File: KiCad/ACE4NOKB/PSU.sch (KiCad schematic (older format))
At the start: 31 parts, among them IC1 LM7805_TO220

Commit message: Reorder chematics.
Signed-off-by: John Bradley <flypie@rocketmail.com>
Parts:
- removed Z10, Z11, Z9: 74AHCT393, Package_DIP:DIP-14_W7.62mm, symbol 74xx:74LS393
- renumbered IC1 to PR1
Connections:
- wire segments 105 -> 99
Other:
- moved on the sheet: Z101B, Z20E, Z21D, Z22D, Z23E, Z24E, Z25E
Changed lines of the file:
@@
 $Descr A4 11693 8268
 encoding utf-8
-Sheet 6 6
+Sheet 7 8
 Title "ACE4NOKB"
-Date "2019-10-24"
+Date "2020-04-30"
 Rev "Alpha"
 Comp "Ontobus"
@@
 	3150 1825 3275 1825
 Wire Wire Line
-	7850 3025 7525 3025
+	7850 3025 6225 3025
 Wire Wire Line
 	4925 1100 5175 1100
 Wire Wire Line
-	7525 3025 7075 3025
-Connection ~ 7525 3025
-Connection ~ 7075 3025
-Wire Wire Line
-	7075 3025 6625 3025
-Connection ~ 6625 3025
-Wire Wire Line
-	6625 3025 6200 3025
-Connection ~ 6200 3025
-Wire Wire Line
-	6200 3025 5775 3025
+	6225 3025 5775 3025
+Connection ~ 6225 3025
 Connection ~ 5775 3025
+Wire Wire Line
+	5775 3025 5325 3025
 Connection ~ 5325 3025
-Connection ~ 3550 3025
+Wire Wire Line
+	5325 3025 4900 3025
+Connection ~ 4900 3025
+Wire Wire Line
+	4900 3025 4475 3025
+Connection ~ 4475 3025
 Connection ~ 2675 3025
 Wire Wire Line
 	2675 3025 2225 3025
 Wire Wire Line
-	7775 4025 7525 4025
-Connection ~ 7525 4025
-Wire Wire Line
-	7525 4025 7075 4025
-Connection ~ 7075 4025
-Wire Wire Line
-	7075 4025 6625 4025
-Connection ~ 6625 4025
-Wire Wire Line
-	6625 4025 6200 4025
-Connection ~ 6200 4025
-Wire Wire Line
-	6200 4025 5775 4025
+	6475 4025 6225 4025
+Connection ~ 6225 4025
+Wire Wire Line
+	6225 4025 5775 4025
 Connection ~ 5775 4025
+Wire Wire Line
+	5775 4025 5325 4025
 Connection ~ 5325 4025
-Connection ~ 3550 4025
+Wire Wire Line
+	5325 4025 4900 4025
+Connection ~ 4900 4025
+Wire Wire Line
+	4900 4025 4475 4025
+Connection ~ 4475 4025
 Connection ~ 2675 4025
 Wire Wire Line
@@
 	3975 1100 3975 1325
 Wire Wire Line
-	3550 3025 3125 3025
-Wire Wire Line
-	3550 4025 3125 4025
-Wire Wire Line
 	3125 3125 3125 3025
-Connection ~ 3125 3025
 Wire Wire Line
 	3125 3025 2675 3025
 Wire Wire Line
 	3125 3925 3125 4025
-Connection ~ 3125 4025
 Wire Wire Line
 	3125 4025 2675 4025
 Wire Wire Line
-	5775 4025 5325 4025
-Wire Wire Line
-	5775 3025 5325 3025
+	4475 4025 4025 4025
+Wire Wire Line
+	4475 3025 4025 3025
 Wire Wire Line
 	1425 1400 1425 1200
@@
 Connection ~ 1425 1700
 Connection ~ 1425 1825
-Wire Wire Line
-	5325 4025 4900 4025
-Wire Wire Line
-	5325 3025 4900 3025
-Connection ~ 4900 4025
-Wire Wire Line
-	4900 4025 4450 4025
-Connection ~ 4900 3025
-Wire Wire Line
-	4900 3025 4450 3025
-Connection ~ 3975 4025
-Wire Wire Line
-	3975 4025 3550 4025
-Connection ~ 3975 3025
-Wire Wire Line
-	3975 3025 3550 3025
-Connection ~ 4450 4025
-Wire Wire Line
-	4450 4025 3975 4025
-Connection ~ 4450 3025
-Wire Wire Line
-	4450 3025 3975 3025
-$Comp
-L 74xx:74LS393 Z9
-U 3 1 5E382F4F
-P 4900 3525
-F 0 "Z9" H 4975 4125 50  0000 R CNN
-F 1 "74AHCT393" H 5125 4225 50  0000 R CNN
-F 2 "Package_DIP:DIP-14_W7.62mm" H 4900 3525 50  0001 C CNN
-F 3 "74xx\\74LS393.pdf" H 4900 3525 50  0001 C CNN
-	3    4900 3525
-	-1   0    0    1
-$EndComp
 $Comp
 L 74xx:74LS74 Z27
@@
 $EndComp
 $Comp
-L 74xx:74LS393 Z11
-U 3 1 5D2736AB
-P 3550 3525
-F 0 "Z11" H 3650 4125 50  0000 R CNN
-F 1 "74AHCT393" H 3775 4350 50  0000 R CNN
-F 2 "Package_DIP:DIP-14_W7.62mm" H 3550 3525 50  0001 C CNN
-F 3 "74xx\\74LS393.pdf" H 3550 3525 50  0001 C CNN
-	3    3550 3525
-	-1   0    0    1
-$EndComp
-$Comp
-L 74xx:74LS393 Z10
-U 3 1 5D1978A5
-P 3975 3525
-F 0 "Z10" H 3875 4125 50  0000 L CNN
-F 1 "74AHCT393" H 3775 4225 50  0000 L CNN
-F 2 "Package_DIP:DIP-14_W7.62mm" H 3975 3525 50  0001 C CNN
-F 3 "74xx\\74LS393.pdf" H 3975 3525 50  0001 C CNN
-	3    3975 3525
-	-1   0    0    1
-$EndComp
-$Comp
 L 74xx:74LS30 Z101
 U 2 1 6372EB23
-P 4450 3525
-F 0 "Z101" H 4575 4125 50  0000 R CNN
-F 1 "74AHCT30D" H 4650 4350 50  0000 R CNN
-F 2 "Package_SO:SOIC-14_3.9x8.7mm_P1.27mm" H 4450 3525 50  0001 C CNN
-F 3 "http://www.ti.com/lit/gpn/sn74LS21" H 4450 3525 50  0001 C CNN
-F 4 "NEXPERIA" H 4450 3525 50  0001 C CNN "Manufacturer_Name"
-F 5 "74AHCT30D" H 4450 3525 50  0001 C CNN "Manufacturer_Part_Number"
-	2    4450 3525
+P 3575 3525
+F 0 "Z101" H 3700 4125 50  0000 R CNN
+F 1 "74AHCT30D" H 3775 4350 50  0000 R CNN
+F 2 "Package_SO:SOIC-14_3.9x8.7mm_P1.27mm" H 3575 3525 50  0001 C CNN
+F 3 "http://www.ti.com/lit/gpn/sn74LS21" H 3575 3525 50  0001 C CNN
+F 4 "NEXPERIA" H 3575 3525 50  0001 C CNN "Manufacturer_Name"
+F 5 "74AHCT30D" H 3575 3525 50  0001 C CNN "Manufacturer_Part_Number"
+	2    3575 3525
 	-1   0    0    1
 $EndComp
@@
 L 74xx:74LS11 Z22
 U 4 1 6989826C
-P 6625 3525
-F 0 "Z22" H 6700 4125 50  0000 R CNN
-F 1 "74AHCT11" H 6825 4225 50  0000 R CNN
-F 2 "Package_DIP:DIP-14_W7.62mm" H 6625 3525 50  0001 C CNN
-F 3 "http://www.ti.com/lit/gpn/sn74LS11" H 6625 3525 50  0001 C CNN
-	4    6625 3525
+P 5325 3525
+F 0 "Z22" H 5400 4125 50  0000 R CNN
+F 1 "74AHCT11" H 5525 4225 50  0000 R CNN
+F 2 "Package_DIP:DIP-14_W7.62mm" H 5325 3525 50  0001 C CNN
+F 3 "http://www.ti.com/lit/gpn/sn74LS11" H 5325 3525 50  0001 C CNN
+	4    5325 3525
 	-1   0    0    1
 $EndComp
@@
 L 74xx:74LS02 Z24
 U 5 1 629F3A79
-P 5325 3525
-F 0 "Z24" H 5425 4125 50  0000 R CNN
-F 1 "SN74AHCT02N" H 5600 4350 50  0000 R CNN
-F 2 "Package_DIP:DIP-14_W7.62mm" H 5325 3525 50  0001 C CNN
-F 3 "http://www.ti.com/lit/gpn/sn74ls02" H 5325 3525 50  0001 C CNN
-	5    5325 3525
-	-1   0    0    1
-$EndComp
-$Comp
-L Regulator_Linear:LM7805_TO220 IC1
+P 4025 3525
+F 0 "Z24" H 4125 4125 50  0000 R CNN
+F 1 "SN74AHCT02N" H 4300 4350 50  0000 R CNN
+F 2 "Package_DIP:DIP-14_W7.62mm" H 4025 3525 50  0001 C CNN
+F 3 "http://www.ti.com/lit/gpn/sn74ls02" H 4025 3525 50  0001 C CNN
+	5    4025 3525
+	-1   0    0    1
+$EndComp
+$Comp
+L Regulator_Linear:LM7805_TO220 PR1
 U 1 1 735D1281
 P 2650 1100
-F 0 "IC1" H 2675 1375 50  0000 C CNN
+F 0 "PR1" H 2675 1375 50  0000 C CNN
 F 1 "LM7805_TO220" H 2675 1275 50  0000 C CNN
 F 2 "Package_TO_SOT_THT:TO-220-3_Vertical" H 2650 1325 50  0001 C CIN
@@
 L 74xx:74LS86 Z23
 U 5 1 6A760723
-P 7525 3525
-F 0 "Z23" H 7250 3450 50  0000 R CNN
-F 1 "74AHCT86" H 7250 3550 50  0000 R CNN
-F 2 "Package_DIP:DIP-14_W7.62mm" H 7525 3525 50  0001 C CNN
-F 3 "74xx/74ls86.pdf" H 7525 3525 50  0001 C CNN
-	5    7525 3525
+P 6225 3525
+F 0 "Z23" H 5950 3450 50  0000 R CNN
+F 1 "74AHCT86" H 5950 3550 50  0000 R CNN
+F 2 "Package_DIP:DIP-14_W7.62mm" H 6225 3525 50  0001 C CNN
+F 3 "74xx/74ls86.pdf" H 6225 3525 50  0001 C CNN
+	5    6225 3525
 	-1   0    0    1
 $EndComp
@@
 L 74xx:74LS11 Z21
 U 4 1 69DE0CE8
-P 7075 3525
-F 0 "Z21" H 6975 4125 50  0000 L CNN
-F 1 "74AHCT11" H 6875 4350 50  0000 L CNN
-F 2 "Package_DIP:DIP-14_W7.62mm" H 7075 3525 50  0001 C CNN
-F 3 "http://www.ti.com/lit/gpn/sn74LS11" H 7075 3525 50  0001 C CNN
-	4    7075 3525
+P 5775 3525
+F 0 "Z21" H 5675 4125 50  0000 L CNN
+F 1 "74AHCT11" H 5575 4350 50  0000 L CNN
+F 2 "Package_DIP:DIP-14_W7.62mm" H 5775 3525 50  0001 C CNN
+F 3 "http://www.ti.com/lit/gpn/sn74LS11" H 5775 3525 50  0001 C CNN
+	4    5775 3525
 	-1   0    0    1
 $EndComp
@@
 L 74xx:74LS02 Z25
 U 5 1 67CF6A6D
-P 5775 3525
-F 0 "Z25" H 5875 4125 50  0000 R CNN
-F 1 "74AHCT02" H 5975 4225 50  0000 R CNN
-F 2 "Package_DIP:DIP-14_W7.62mm" H 5775 3525 50  0001 C CNN
-F 3 "http://www.ti.com/lit/gpn/sn74ls02" H 5775 3525 50  0001 C CNN
-	5    5775 3525
+P 4475 3525
+F 0 "Z25" H 4575 4125 50  0000 R CNN
+F 1 "74AHCT02" H 4675 4225 50  0000 R CNN
+F 2 "Package_DIP:DIP-14_W7.62mm" H 4475 3525 50  0001 C CNN
+F 3 "http://www.ti.com/lit/gpn/sn74ls02" H 4475 3525 50  0001 C CNN
+	5    4475 3525
 	-1   0    0    1
 $EndComp
@@
 L 74xx:74LS08 Z20
 U 5 1 68B9DD2C
-P 6200 3525
-F 0 "Z20" H 6300 4125 50  0000 R CNN
-F 1 "74AHCT08" H 6400 4350 50  0000 R CNN
-F 2 "Package_DIP:DIP-14_W7.62mm" H 6200 3525 50  0001 C CNN
-F 3 "http://www.ti.com/lit/gpn/sn74LS08" H 6200 3525 50  0001 C CNN
-	5    6200 3525
+P 4900 3525
+F 0 "Z20" H 5000 4125 50  0000 R CNN
+F 1 "74AHCT08" H 5100 4350 50  0000 R CNN
+F 2 "Package_DIP:DIP-14_W7.62mm" H 4900 3525 50  0001 C CNN
+F 3 "http://www.ti.com/lit/gpn/sn74LS08" H 4900 3525 50  0001 C CNN
+	5    4900 3525
 	-1   0    0    1
 $EndComp
@@
 	-1   0    0    1
 $EndComp
+Wire Wire Line
+	4025 3025 3575 3025
+Connection ~ 4025 3025
+Connection ~ 3125 3025
+Connection ~ 3575 3025
+Wire Wire Line
+	3575 3025 3125 3025
+Wire Wire Line
+	3125 4025 3575 4025
+Connection ~ 3125 4025
+Connection ~ 4025 4025
+Connection ~ 3575 4025
+Wire Wire Line
+	3575 4025 4025 4025
 $EndSCHEMATC

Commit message: Address inconsistencies between 3,4,5. Renumber part to reflect version. Relocate Z80 parts library to separate repository.
https://github.com/flypie/Z80-CPU-for-KiCAD

Signed-off-by: John Bradley <flypie@rocketmail.com>
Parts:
- added Z301: 74HCT21, Package_DIP:DIP-14_W7.62mm_Socket, symbol 74xx:74LS21
- added Z302: 74HCT32, Package_DIP:DIP-14_W7.62mm_Socket, symbol 74xx:74LS32
- added Z400: 74LS393, Package_DIP:DIP-14_W7.62mm_Socket, symbol 74xx:74LS393
- POWER-9V-DC1: footprint cuipj:CUI_PJ-036C -> SamacSys_Parts:163179PHEX; symbol Connector_Generic:Conn_01x02 -> SamacSys_Parts:163-179PH-EX
- Z19, Z20, Z21, Z22, Z23, Z24, Z25, Z27: footprint Package_DIP:DIP-14_W7.62mm -> Package_DIP:DIP-14_W7.62mm_Socket
- Z201: renamed from Z101; footprint Package_SO:SOIC-14_3.9x8.7mm_P1.27mm -> Package_DIP:DIP-14_W7.62mm_Socket
- Z306: renamed from Z102; footprint Package_DIP:DIP-14_W7.62mm -> Package_DIP:DIP-14_W7.62mm_Socket
- Z307: renamed from Z100; footprint Package_DIP:DIP-16_W7.62mm -> Package_DIP:DIP-16_W7.62mm_Socket
- Z308: renamed from Z104; footprint Package_SO:SOIC-14_3.9x8.7mm_P1.27mm -> Package_DIP:DIP-14_W7.62mm_Socket
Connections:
- net labels added: +9Vus
- no-connect marks 0 -> 1
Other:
- moved on the sheet: C10, C11, C12, C13, C14, C15, C16, C17, C18, C19, C20, C21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

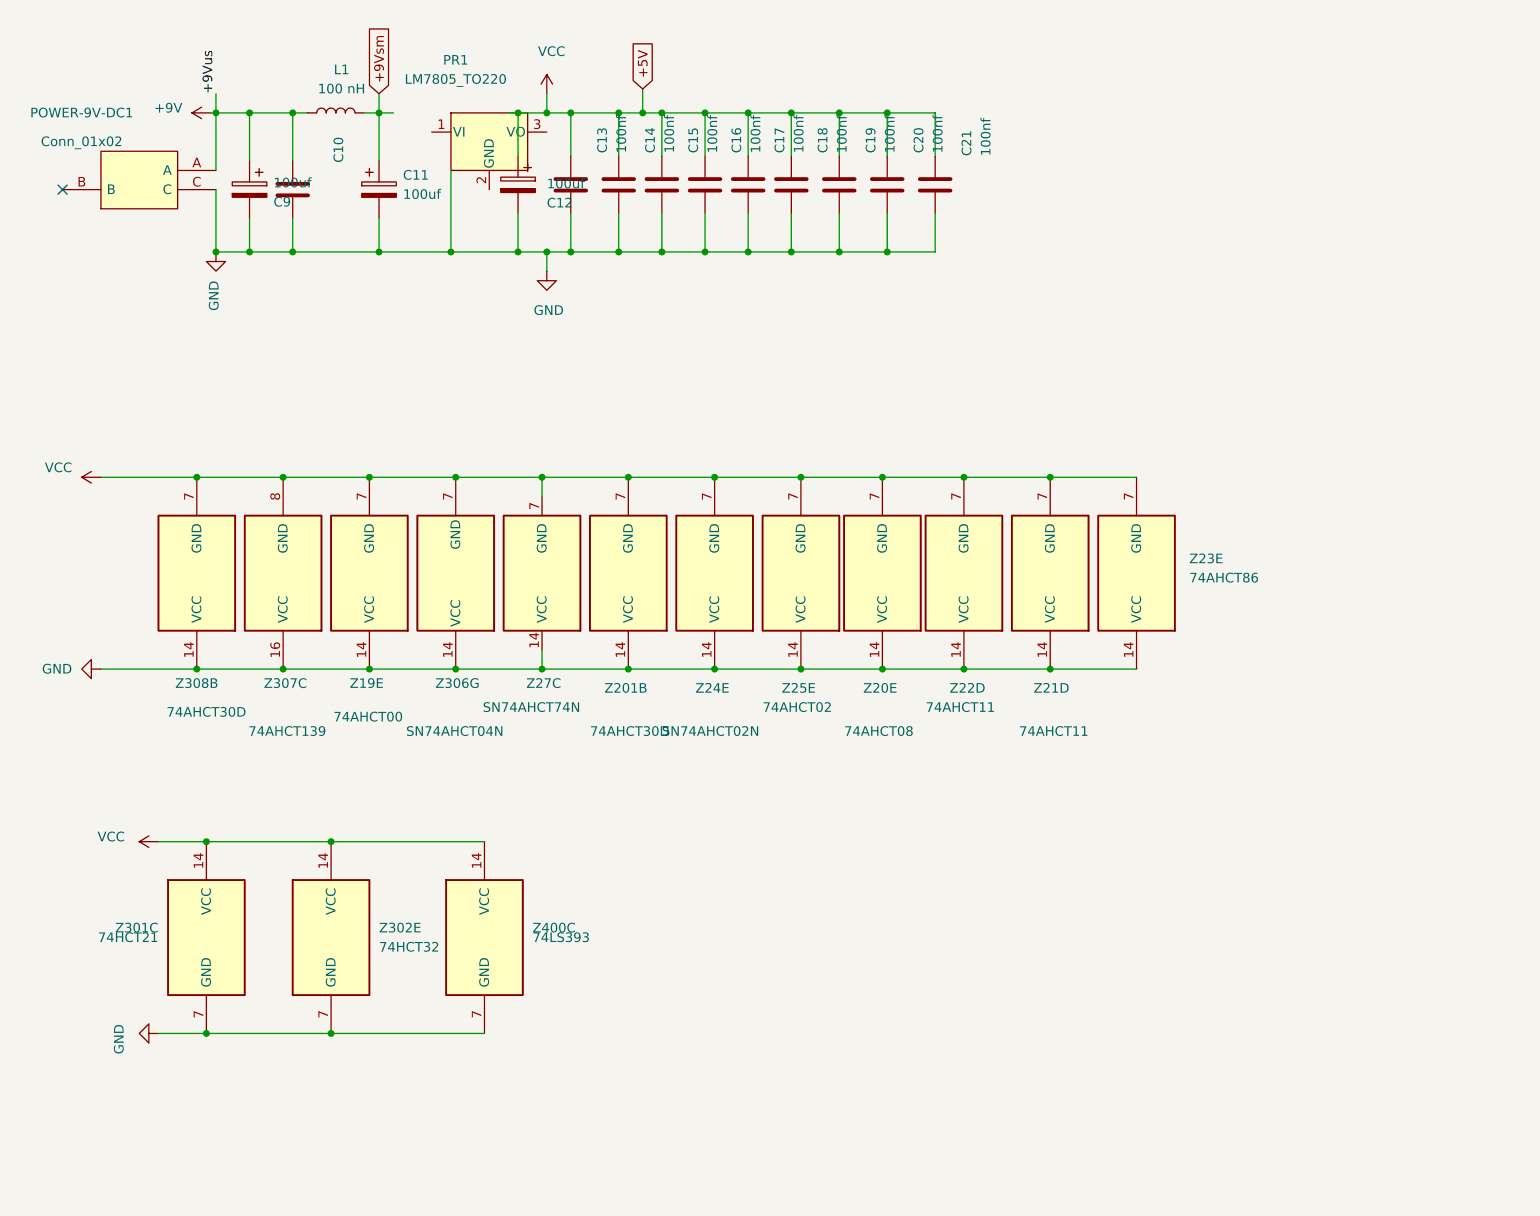
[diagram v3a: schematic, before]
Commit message: Rearrange boards 4 & 5. Make IC numbering consistent.
Signed-off-by: John Bradley <flypie@rocketmail.com>
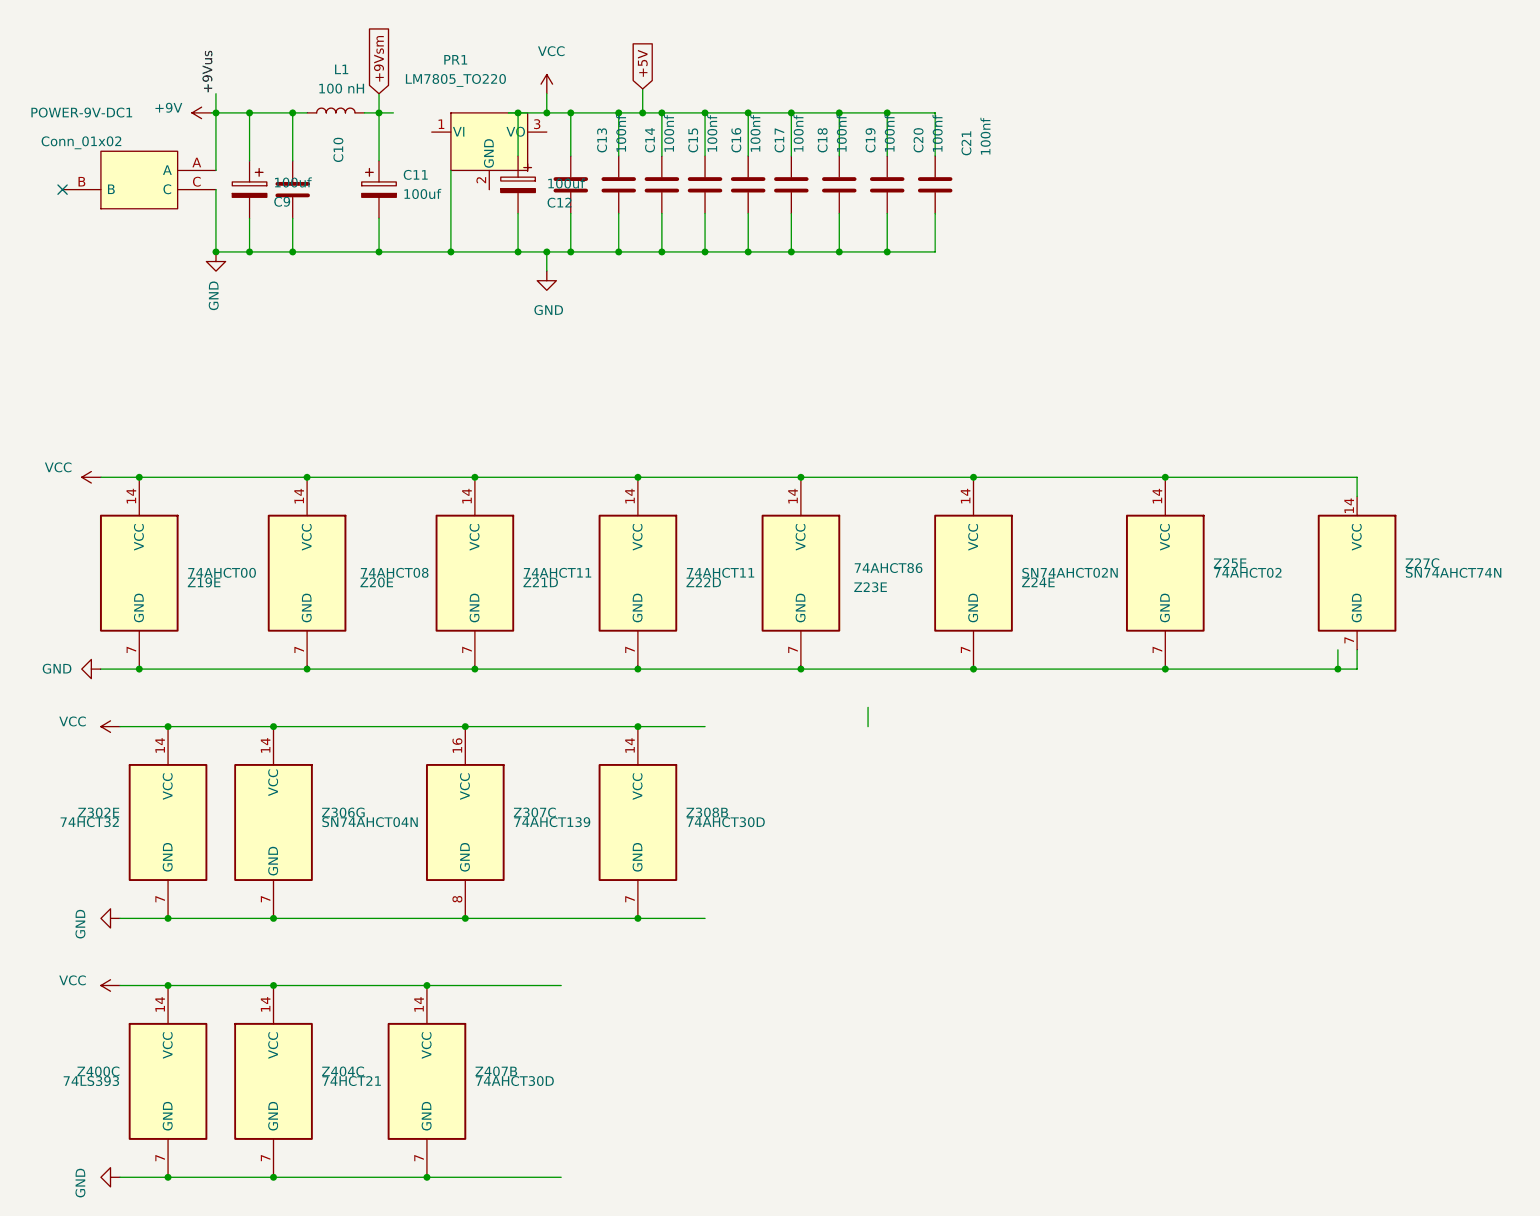
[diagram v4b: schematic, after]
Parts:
- removed Z301: 74HCT21, Package_DIP:DIP-14_W7.62mm_Socket, symbol 74xx:74LS21
- added Z404: 74HCT21, Package_DIP:DIP-14_W7.62mm_Socket, symbol 74xx:74LS21
- renumbered Z201 to Z407
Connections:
- wire segments 99 -> 106
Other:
- moved on the sheet: Z19E, Z20E, Z21D, Z22D, Z23E, Z24E, Z25E, Z27C, Z302E, Z306G, Z307C, Z308B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
